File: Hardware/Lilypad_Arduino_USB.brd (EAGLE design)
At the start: 50.8 x 50.8 mm, 46 parts, among them U1 MCP73831, U2 MIC5219, U3 ATMEGA32U41:1, Y1 8MHz

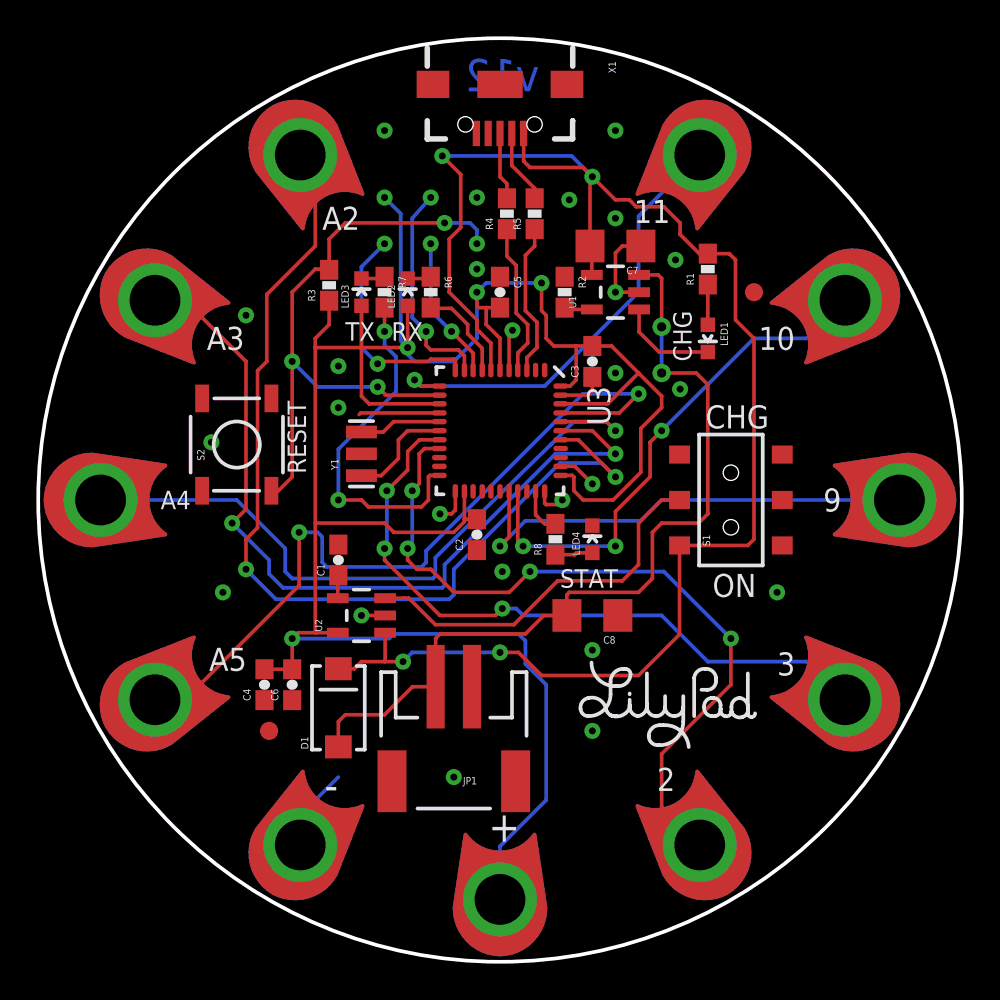
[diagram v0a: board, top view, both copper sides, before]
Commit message: More updated packages
1.) New 0603 LED packages
2.) New resonator package
3.) Moved reset button over to allow silk to be correct size.
4.) Added attribution to board file
5.) Minor trace reroutes for new packages
6.) New 32u4 package variant that changes paste layer.
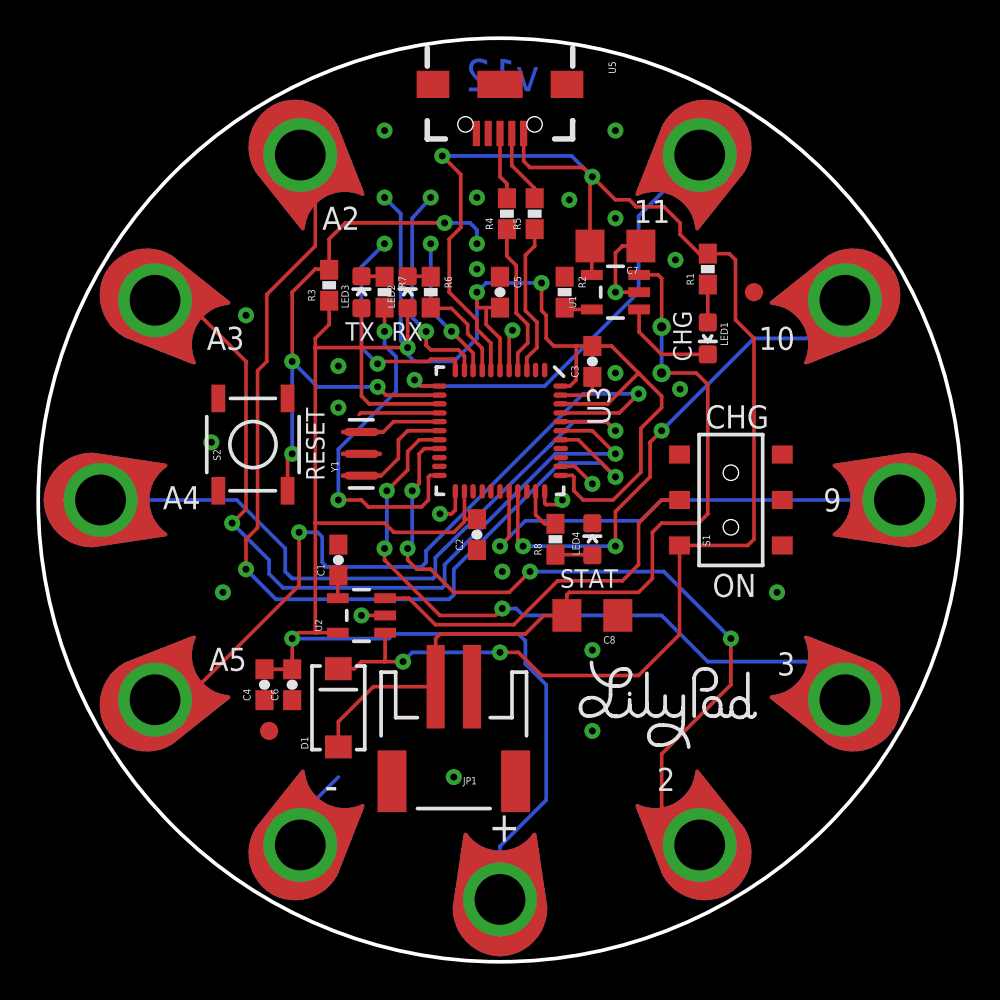
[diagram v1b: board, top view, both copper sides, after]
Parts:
- removed X1: (no value), Testing:USB-AB-MICRO-SMD_V03
- added FRAME1: FRAME-LETTER, SparkFun-Aesthetics:CREATIVE_COMMONS
- added U5: (no value), SparkFun-Connectors:USB-AB-MICRO-SMD_V03
- S1: value SWITCH-DPDTSMD -> (none)
- U3: value ATMEGA32U41:1 -> ATMEGA32U41:1-LESS_PASTE; device Testing:QFN-44-NOPAD_1:1 -> Testing:QFN-44-NOPAD_1:1-LESS_PASTE
- moved U$5 15.2 mm to (0.00, -6.35)
- moved S2 0.89 mm to (-13.6, 3.05)
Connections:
- net 5V: now also U5.VBUS1; no longer X1.VBUS1
- net GND: now also U5.GND1; no longer X1.GND1
- net N$19: now also U5.D-1; no longer X1.D-1
- net N$20: now also U5.D+1; no longer X1.D+1
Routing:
- net RESET: track 34.2 -> 33.6 mm, vias 4 -> 5
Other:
- board text added: "Mike Hord"
- board text added: "Revised by: Kade Jensen"

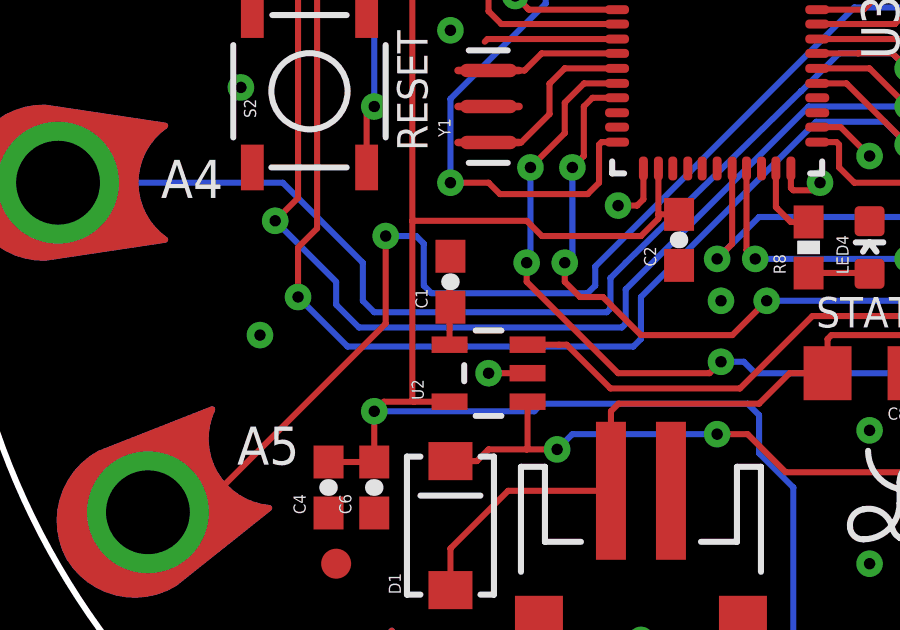
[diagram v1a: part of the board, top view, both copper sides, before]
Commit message: Fixing wonky trace under C1
Correcting a trace overshoot on C1 near vreg.
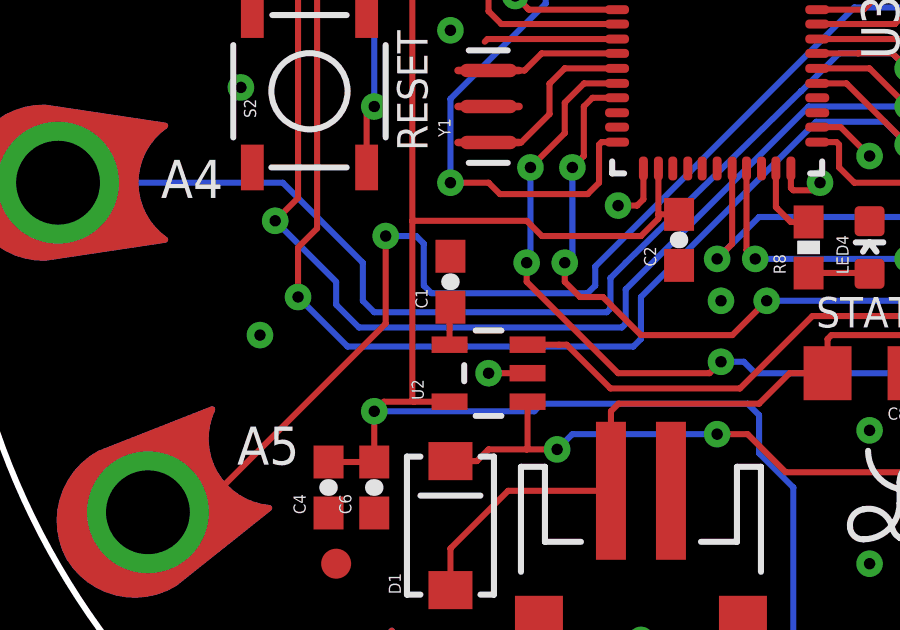
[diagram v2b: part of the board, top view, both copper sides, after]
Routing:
- net N$8: track 2.71 -> 1.26 mm
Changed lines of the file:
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@@
 <contactref element="U2" pad="4"/>
 <contactref element="C1" pad="1"/>
-<wire x1="-8.920096875" y1="-5.4" x2="-8.92009375" y2="-3.4201" width="0.2032" layer="1"/>
-<wire x1="-8.92009375" y1="-3.4201" x2="-8.889996875" y2="-4.151996875" width="0.2032" layer="1"/>
+<wire x1="-8.920096875" y1="-5.4" x2="-8.920096875" y2="-4.182096875" width="0.2032" layer="1"/>
+<wire x1="-8.920096875" y1="-4.182096875" x2="-8.889996875" y2="-4.151996875" width="0.254" layer="1"/>
 </signal>
 <signal name="N$9">

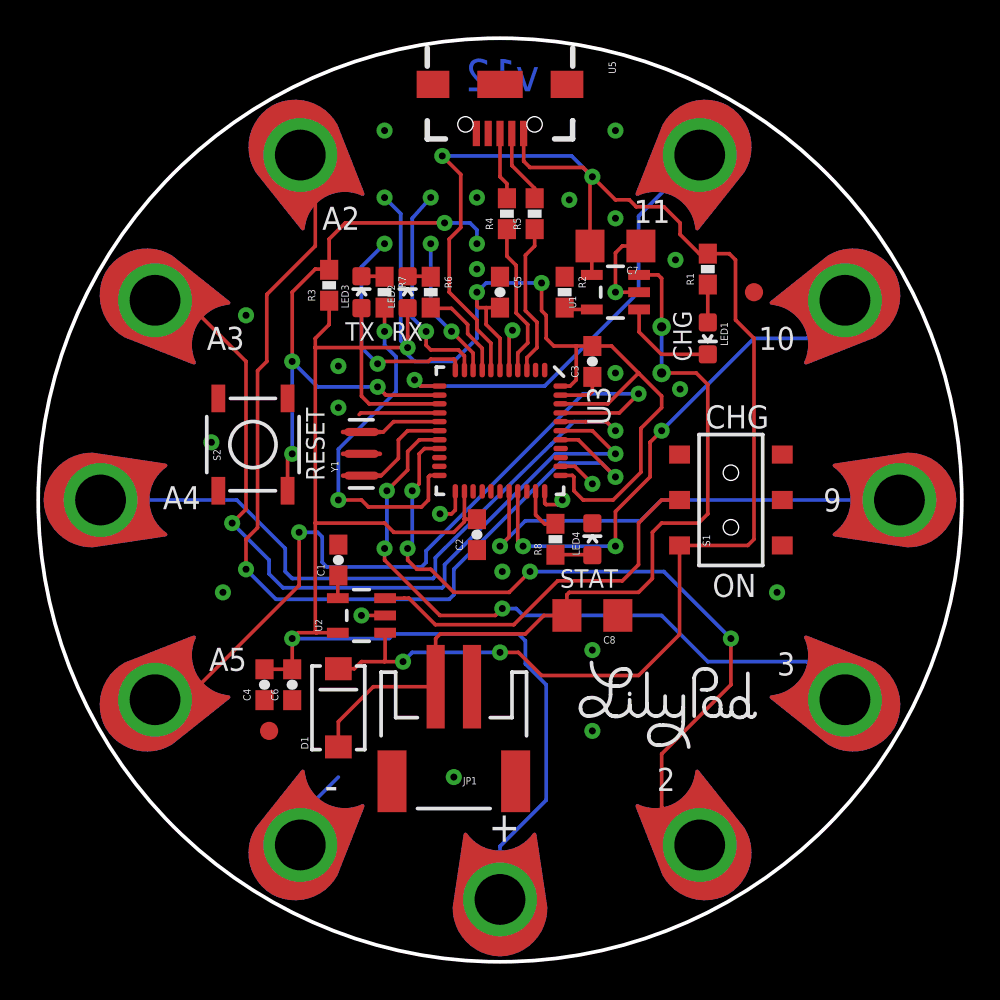
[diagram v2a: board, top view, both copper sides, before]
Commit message: Updated silk and two traces
1.) Changed bottom silk to not interfere with vias
2.) Changed two traces to be more efficient
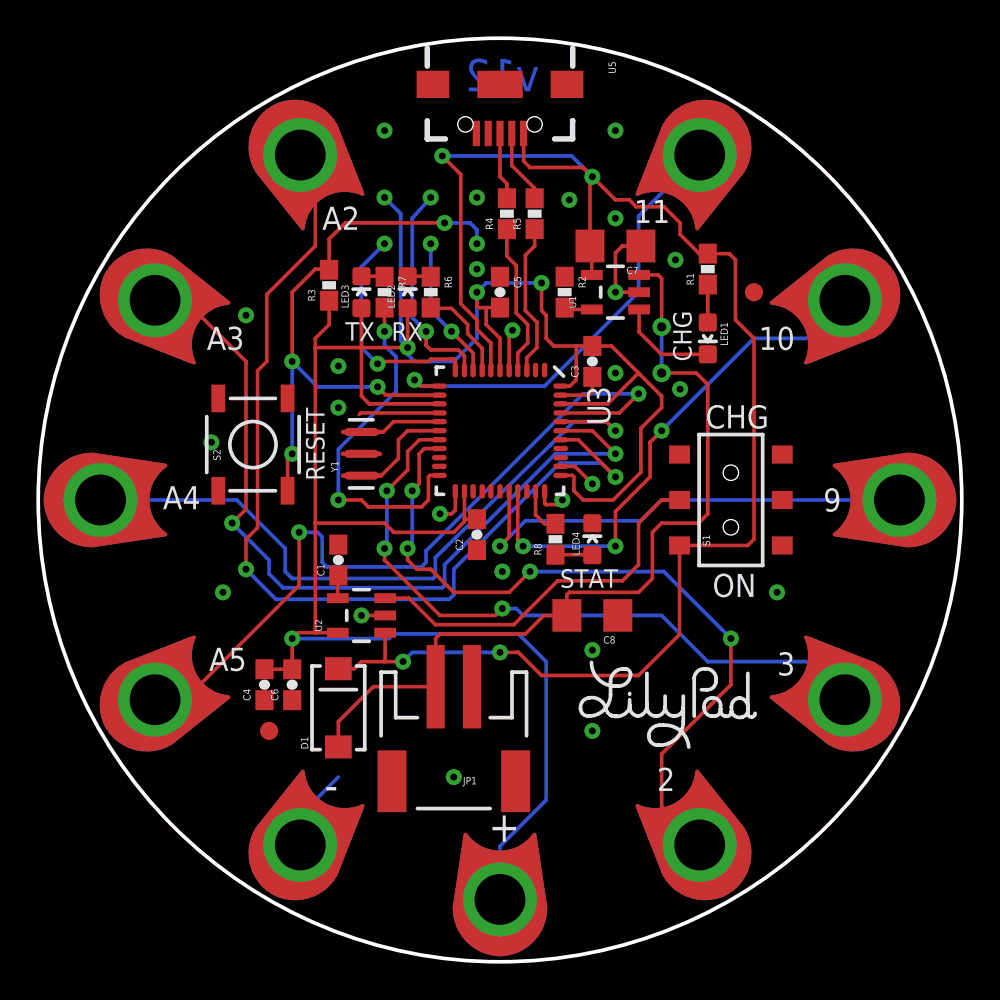
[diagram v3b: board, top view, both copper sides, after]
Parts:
- removed U$6: (no value), SparkFun-Aesthetics:SFE-LOGO-FLAME
- added U$7: (no value), SparkFun-Aesthetics:SFE_LOGO_FLAME_.2
- moved U$5 11.6 mm to (-3.81, 4.57)
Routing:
- net 5V: track 90.6 -> 90.0 mm
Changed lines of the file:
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@@
 <layers>
 <layer number="1" name="Top" color="4" fill="1" visible="yes" active="yes"/>
-<layer number="2" name="Route2" color="1" fill="3" visible="yes" active="yes"/>
-<layer number="15" name="Route15" color="4" fill="6" visible="yes" active="yes"/>
+<layer number="2" name="Route2" color="1" fill="3" visible="no" active="yes"/>
+<layer number="15" name="Route15" color="4" fill="6" visible="no" active="yes"/>
 <layer number="16" name="Bottom" color="1" fill="1" visible="yes" active="yes"/>
 <layer number="17" name="Pads" color="2" fill="1" visible="yes" active="yes"/>
@@
 <layer number="23" name="tOrigins" color="15" fill="1" visible="yes" active="yes"/>
 <layer number="24" name="bOrigins" color="15" fill="1" visible="yes" active="yes"/>
-<layer number="25" name="tNames" color="7" fill="1" visible="yes" active="yes"/>
-<layer number="26" name="bNames" color="7" fill="1" visible="yes" active="yes"/>
-<layer number="27" name="tValues" color="7" fill="1" visible="yes" active="yes"/>
-<layer number="28" name="bValues" color="7" fill="1" visible="yes" active="yes"/>
-<layer number="29" name="tStop" color="7" fill="3" visible="yes" active="yes"/>
-<layer number="30" name="bStop" color="7" fill="6" visible="yes" active="yes"/>
-<layer number="31" name="tCream" color="7" fill="4" visible="yes" active="yes"/>
-<layer number="32" name="bCream" color="7" fill="5" visible="yes" active="yes"/>
-<layer number="39" name="tKeepout" color="4" fill="11" visible="yes" active="yes"/>
-<layer number="40" name="bKeepout" color="1" fill="11" visible="yes" active="yes"/>
-<layer number="41" name="tRestrict" color="4" fill="10" visible="yes" active="yes"/>
-<layer number="42" name="bRestrict" color="1" fill="10" visible="yes" active="yes"/>
-<layer number="44" name="Drills" color="7" fill="1" visible="yes" active="yes"/>
+<layer number="25" name="tNames" color="7" fill="1" visible="no" active="yes"/>
+<layer number="26" name="bNames" color="7" fill="1" visible="no" active="yes"/>
+<layer number="27" name="tValues" color="7" fill="1" visible="no" active="yes"/>
+<layer number="28" name="bValues" color="7" fill="1" visible="no" active="yes"/>
+<layer number="29" name="tStop" color="7" fill="3" visible="no" active="yes"/>
+<layer number="30" name="bStop" color="7" fill="6" visible="no" active="yes"/>
+<layer number="31" name="tCream" color="7" fill="4" visible="no" active="yes"/>
+<layer number="32" name="bCream" color="7" fill="5" visible="no" active="yes"/>
+<layer number="39" name="tKeepout" color="4" fill="11" visible="no" active="yes"/>
+<layer number="40" name="bKeepout" color="1" fill="11" visible="no" active="yes"/>
+<layer number="41" name="tRestrict" color="4" fill="10" visible="no" active="yes"/>
+<layer number="42" name="bRestrict" color="1" fill="10" visible="no" active="yes"/>
+<layer number="44" name="Drills" color="7" fill="1" visible="no" active="yes"/>
 <layer number="45" name="Holes" color="7" fill="1" visible="yes" active="yes"/>
-<layer number="46" name="Milling" color="3" fill="1" visible="yes" active="yes"/>
+<layer number="46" name="Milling" color="3" fill="1" visible="no" active="yes"/>
 <layer number="51" name="tDocu" color="6" fill="1" visible="yes" active="yes"/>
 <layer number="3" name="Route3" color="4" fill="3" visible="no" active="no"/>
@@
 <layer number="106" name="bPlate" color="7" fill="1" visible="no" active="no"/>
 <layer number="107" name="Crop" color="7" fill="1" visible="no" active="no"/>
-<layer number="108" name="tplace-old" color="10" fill="1" visible="yes" active="yes"/>
-<layer number="109" name="ref-old" color="11" fill="1" visible="yes" active="yes"/>
+<layer number="108" name="tplace-old" color="10" fill="1" visible="no" active="yes"/>
+<layer number="109" name="ref-old" color="11" fill="1" visible="no" active="yes"/>
 <layer number="116" name="Patch_BOT" color="9" fill="4" visible="no" active="no"/>
 <layer number="121" name="_tsilk" color="7" fill="1" visible="no" active="no"/>
@@
 <layer number="144" name="Drill_legend" color="7" fill="1" visible="no" active="no"/>
 <layer number="151" name="HeatSink" color="7" fill="1" visible="no" active="no"/>
-<layer number="199" name="Contour" color="7" fill="1" visible="yes" active="yes"/>
+<layer number="199" name="Contour" color="7" fill="1" visible="no" active="yes"/>
 <layer number="200" name="200bmp" color="1" fill="10" visible="no" active="no"/>
 <layer number="201" name="201bmp" color="2" fill="1" visible="no" active="no"/>
@@
 <element name="JP3" library="SparkFun" package="FIDUCIAL-1X2" value="FIDUCIAL1X2" x="13.969996875" y="11.429996875"/>
 <element name="U$1" library="LilyPad-Wearables" package="LOGO-LPA" value="LOGO-LPLPA" x="0" y="0" rot="MR0"/>
-<element name="U$5" library="SparkFun" package="OSHW-LOGO-M" value="OSHW-LOGOM" x="0" y="-6.35" rot="MR0"/>
-<element name="U$6" library="SparkFun-Aesthetics" package="SFE-LOGO-FLAME" value="" x="0.762" y="2.794" rot="MR0"/>
+<element name="U$5" library="SparkFun" package="OSHW-LOGO-M" value="OSHW-LOGOM" x="-3.81" y="4.572" rot="MR0"/>
 <element name="FRAME1" library="SparkFun-Aesthetics" package="CREATIVE_COMMONS" value="FRAME-LETTER" x="-113.30645" y="0"/>
 <element name="D1" library="SparkFun-DiscreteSemi" package="SMA-DIODE" value="B340A" x="-8.89" y="-11.43" rot="R90">
@@
 <attribute name="PROD_ID" value="CONN-11794" x="0" y="22.86" size="1.778" layer="27" font="vector" ratio="15" rot="R270" display="off"/>
 </element>
+<element name="U$7" library="SparkFun-Aesthetics" package="SFE_LOGO_FLAME_.2" value="" x="5.08" y="2.032" rot="MR0"/>
 </elements>
 <signals>
@@
 <wire x1="-6.096" y1="-7.619996875" x2="-5.842" y2="-7.365996875" width="0.2032" layer="16"/>
 <wire x1="-5.842" y1="-7.365996875" x2="1.016" y2="-7.365996875" width="0.2032" layer="16"/>
-<wire x1="1.016" y1="-7.365996875" x2="1.397" y2="-7.746996875" width="0.2032" layer="16"/>
-<wire x1="1.397" y1="-7.746996875" x2="1.396996875" y2="-9.016996875" width="0.2032" layer="16"/>
-<wire x1="1.396996875" y1="-9.016996875" x2="2.539996875" y2="-10.159996875" width="0.2032" layer="16"/>
-<wire x1="2.539996875" y1="-10.159996875" x2="2.539996875" y2="-16.509996875" width="0.2032" layer="16"/>
+<wire x1="2.539996875" y1="-8.88999375" x2="2.539996875" y2="-16.509996875" width="0.2032" layer="16"/>
 <wire x1="2.539996875" y1="-16.509996875" x2="0" y2="-19.04999375" width="0.2032" layer="16"/>
 <wire x1="0" y1="-19.04999375" x2="0" y2="-21.96999375" width="0.2032" layer="16"/>
@@
 <wire x1="-10.159996875" y1="8.382" x2="-10.15999375" y2="8.381996875" width="0.2032" layer="1"/>
 <wire x1="-10.159996875" y1="8.382" x2="-10.159996875" y2="-1.27" width="0.2032" layer="1"/>
+<wire x1="2.539996875" y1="-8.88999375" x2="1.016" y2="-7.365996875" width="0.2032" layer="16"/>
 </signal>
 <signal name="N$8">
@@
 <via x="-3.175" y="18.923" extent="1-16" drill="0.381"/>
 <wire x1="-1.27" y1="9.398" x2="-1.27" y2="9.906" width="0.2032" layer="1"/>
-<wire x1="-1.27" y1="9.906" x2="-2.794" y2="11.43" width="0.2032" layer="1"/>
-<wire x1="-2.794" y1="11.43" x2="-2.794" y2="14.351" width="0.2032" layer="1"/>
-<wire x1="-2.794" y1="14.351" x2="-2.159" y2="14.986" width="0.2032" layer="1"/>
 <wire x1="1.300003125" y1="18.638996875" x2="1.651" y2="18.288" width="0.2032" layer="1"/>
 <wire x1="-3.175" y1="18.923" x2="3.937" y2="18.923" width="0.2032" layer="16"/>
 <wire x1="3.937" y1="18.923" x2="5.08" y2="17.78" width="0.2032" layer="16"/>
-<wire x1="-2.159" y1="14.986" x2="-2.159" y2="17.907" width="0.2032" layer="1"/>
 <wire x1="-2.159" y1="17.907" x2="-3.175" y2="18.923" width="0.2032" layer="1"/>
 <wire x1="1.651" y1="18.288" x2="4.572" y2="18.288" width="0.2032" layer="1"/>
@@
 <wire x1="1.300003125" y1="18.638996875" x2="1.300003125" y2="20.159996875" width="0.2032" layer="1"/>
 <wire x1="1.300003125" y1="20.159996875" x2="1.3" y2="20.16" width="0.2032" layer="1"/>
+<wire x1="-2.159" y1="17.907" x2="-2.159" y2="10.795" width="0.2032" layer="1"/>
+<wire x1="-2.159" y1="10.795" x2="-1.27" y2="9.906" width="0.2032" layer="1"/>
 </signal>
 <signal name="N$19">
